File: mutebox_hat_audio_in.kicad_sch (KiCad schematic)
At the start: 23 parts, among them J1 GPIO, U1 CAT24C256, U2 74LVC157, U3 PCM1862DBT

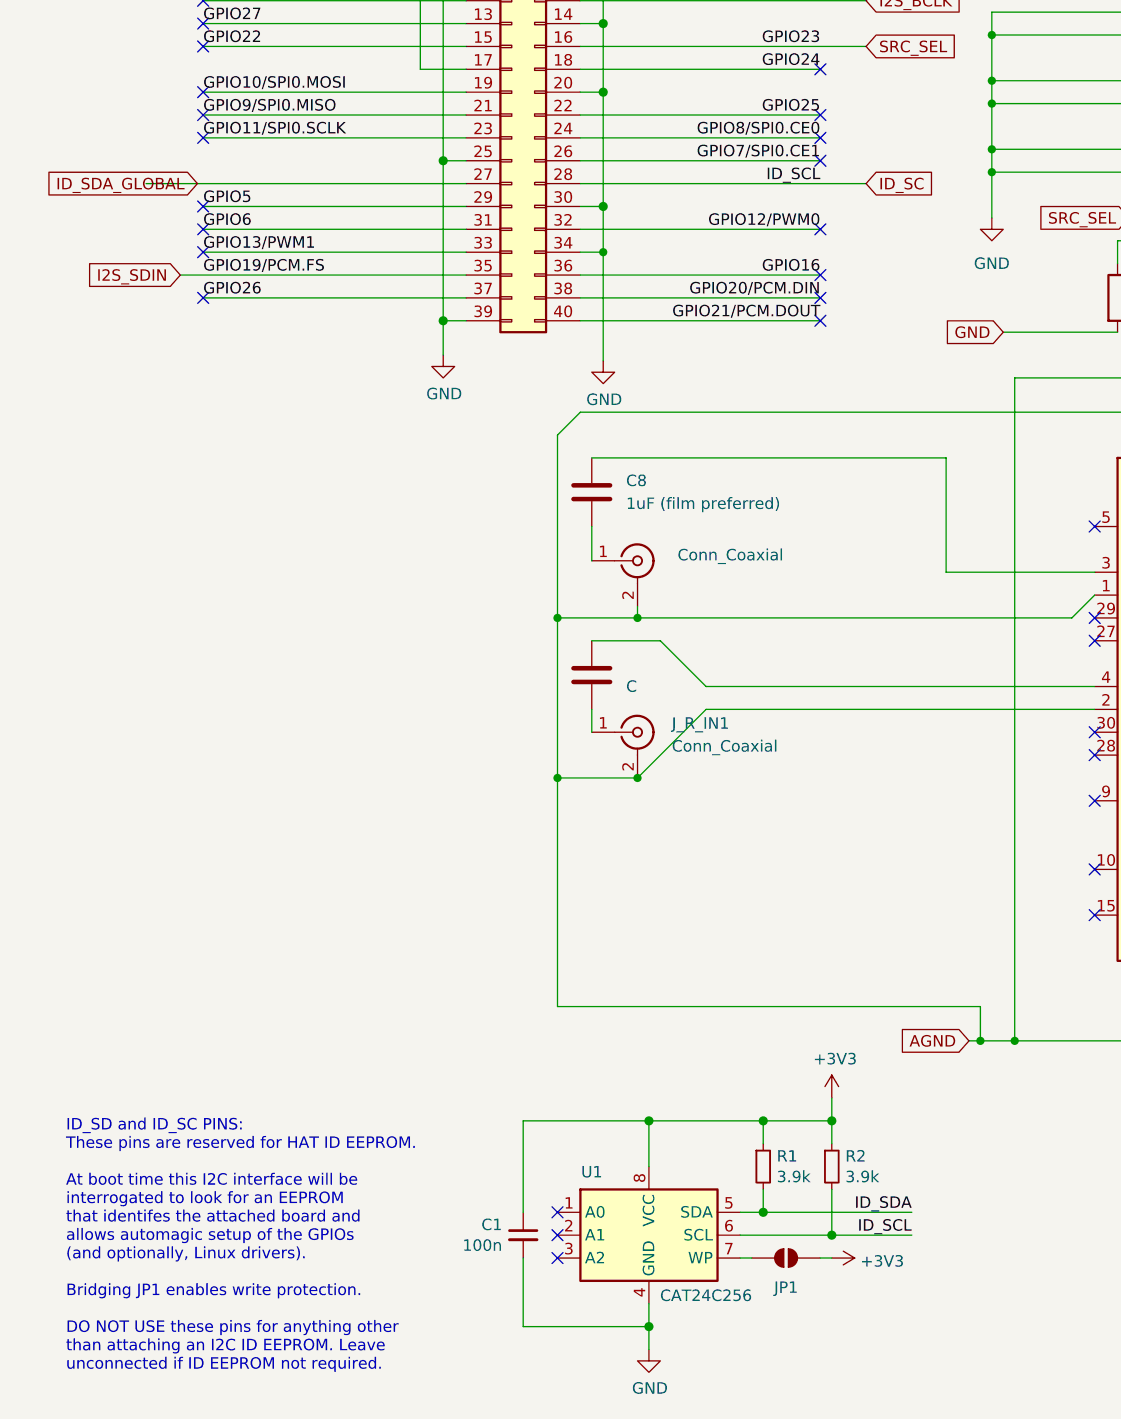
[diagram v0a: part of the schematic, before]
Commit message: Added footprint assignments
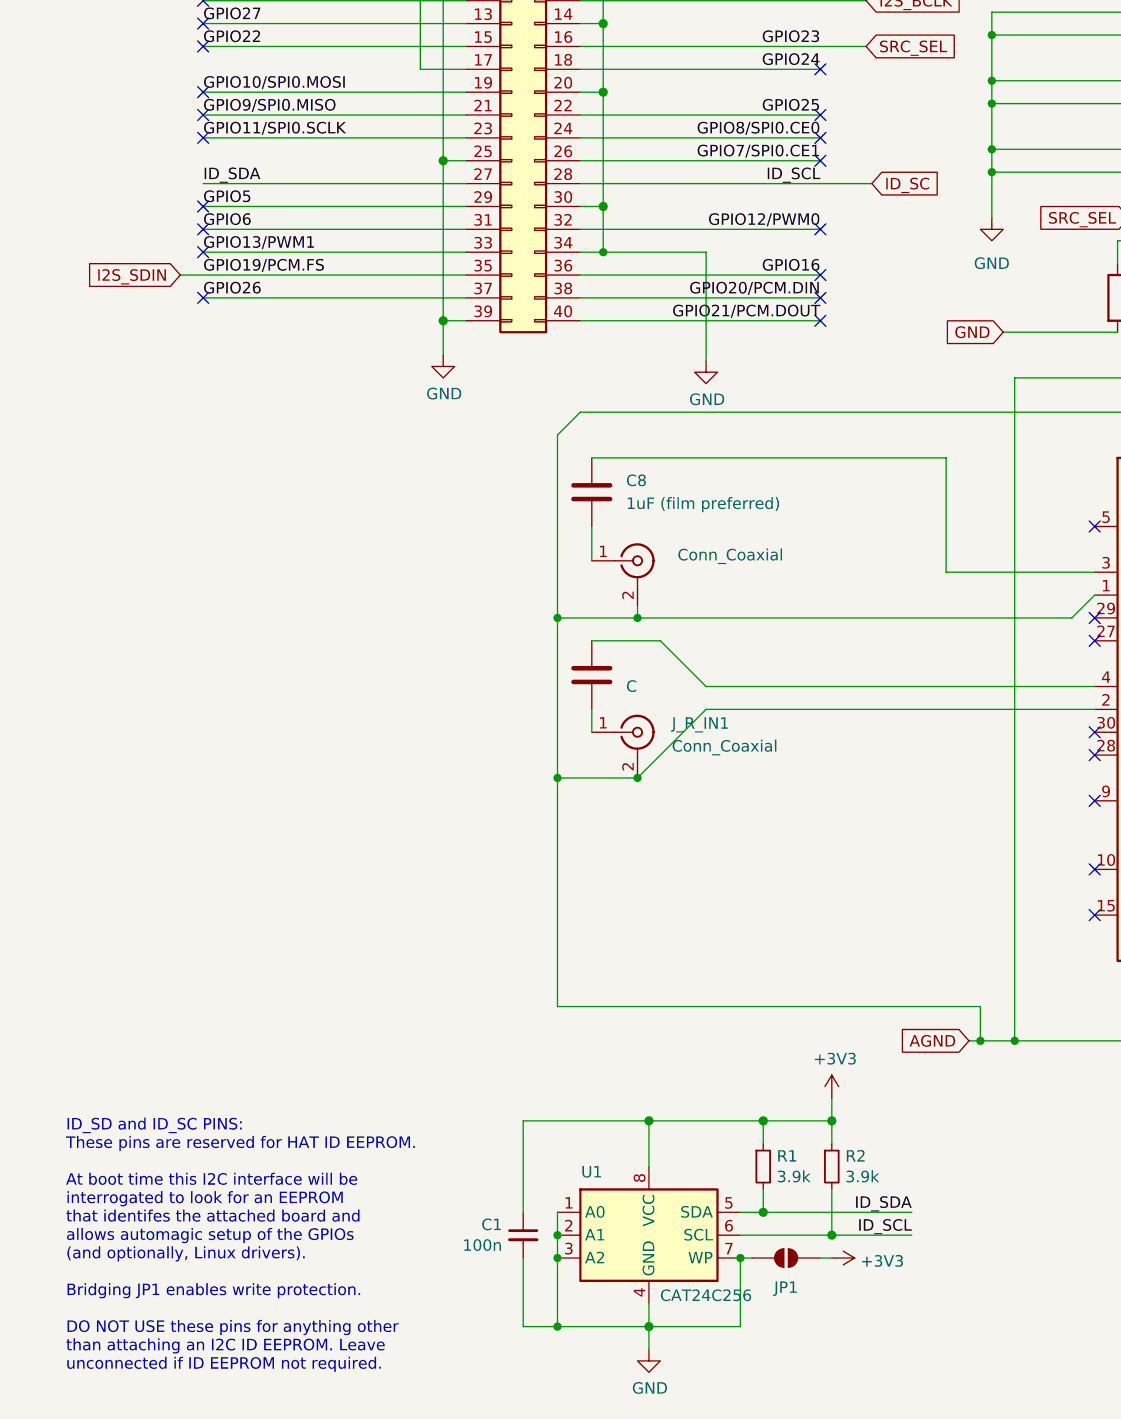
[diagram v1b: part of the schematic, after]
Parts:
- C1, C10, C12, C3, C8, C9, R1, R10, R2, R3, R4, R5, R6, R8, R9: footprint (none) -> Resistor_SMD:R_0805_2012Metric_Pad1.20x1.40mm_HandSolder
- FB1: footprint (none) -> Inductor_SMD:L_0805_2012Metric_Pad1.05x1.20mm_HandSolder
- U1: footprint (none) -> Package_SO:SOIC-8_3.9x4.9mm_P1.27mm
- U2: footprint (none) -> Package_TO_SOT_SMD:SOT-23-5
- U3: footprint Package_SO:TSSOP-30_4.4x7.8mm_P0.5mm -> Package_SO:TSSOP-32_6.1x11mm_P0.65mm
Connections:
- net ID_SDA_GLOBAL is gone; now on net ID_SDA: J1.27 (Pin_27)
- net GND: now also JP1.1 (A), U1.1 (A0), U1.2 (A1), U1.3 (A2), U1.7 (WP)
- no-connect marks 39 -> 36
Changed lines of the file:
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@@
 	)
 	(junction
+		(at 71.12 180.34)
+		(diameter 0)
+		(color 0 0 0 0)
+	)
+	(junction
 		(at 119.38 44.45)
 		(diameter 0)
@@
 	)
 	(junction
+		(at 71.12 187.96)
+		(diameter 0)
+		(color 0 0 0 0)
+	)
+	(junction
+		(at 71.12 177.8)
+		(diameter 0)
+		(color 0 0 0 0)
+	)
+	(junction
 		(at 76.2 63.5)
 		(diameter 1.016)
@@
 	)
 	(junction
+		(at 91.44 180.34)
+		(diameter 0)
+		(color 0 0 0 0)
+	)
+	(junction
 		(at 76.2 33.02)
 		(diameter 0)
@@
 	)
 	(no_connect
-		(at 71.12 175.26)
-	)
-	(no_connect
-		(at 71.12 177.8)
-	)
-	(no_connect
-		(at 71.12 180.34)
-	)
-	(no_connect
 		(at 100.33 53.34)
 	)
@@
 	(wire
 		(pts
-			(xy 25.4 60.96) (xy 60.96 60.96)
-		)
-		(stroke
-			(width 0)
-			(type default)
-		)
-	)
-	(wire
-		(pts
 			(xy 179.07 72.39) (xy 179.07 26.67)
 		)
@@
 	(wire
 		(pts
-			(xy 76.2 68.58) (xy 76.2 80.645)
+			(xy 87.63 68.58) (xy 87.63 80.645)
 		)
 		(stroke
@@
 	(wire
 		(pts
+			(xy 31.75 60.96) (xy 60.96 60.96)
+		)
+		(stroke
+			(width 0)
+			(type default)
+		)
+	)
+	(wire
+		(pts
 			(xy 162.56 34.29) (xy 168.91 34.29)
 		)
@@
 	(wire
 		(pts
+			(xy 71.12 175.26) (xy 71.12 177.8)
+		)
+		(stroke
+			(width 0)
+			(type default)
+		)
+	)
+	(wire
+		(pts
 			(xy 81.28 165.1) (xy 81.28 170.18)
 		)
@@
 	(wire
 		(pts
+			(xy 73.66 60.96) (xy 106.045 60.96)
+		)
+		(stroke
+			(width 0)
+			(type default)
+		)
+	)
+	(wire
+		(pts
 			(xy 193.04 128.27) (xy 193.04 142.24)
 		)
@@
 	(wire
 		(pts
-			(xy 29.21 71.12) (xy 60.96 71.12)
+			(xy 173.99 81.915) (xy 173.99 82.55)
 		)
 		(stroke
 			(width 0)
-			(type solid)
+			(type default)
 		)
 	)
 	(wire
 		(pts
-			(xy 173.99 81.915) (xy 173.99 82.55)
+			(xy 71.12 187.96) (xy 81.28 187.96)
 		)
 		(stroke
 			(width 0)
-			(type default)
+			(type solid)
 		)
 	)
@@
 	(wire
 		(pts
+			(xy 87.63 68.58) (xy 76.2 68.58)
+		)
+		(stroke
+			(width 0)
+			(type default)
+		)
+	)
+	(wire
+		(pts
 			(xy 184.15 128.27) (xy 193.04 128.27)
 		)
@@
 	(wire
 		(pts
+			(xy 71.12 180.34) (xy 71.12 187.96)
+		)
+		(stroke
+			(width 0)
+			(type default)
+		)
+	)
+	(wire
+		(pts
 			(xy 120.65 77.47) (xy 133.35 77.47)
 		)
@@
 	(wire
 		(pts
+			(xy 29.21 71.12) (xy 60.96 71.12)
+		)
+		(stroke
+			(width 0)
+			(type default)
+		)
+	)
+	(wire
+		(pts
 			(xy 67.31 165.1) (xy 67.31 175.26)
 		)
@@
 	(wire
 		(pts
-			(xy 67.31 187.96) (xy 81.28 187.96)
+			(xy 67.31 187.96) (xy 71.12 187.96)
 		)
 		(stroke
@@
 	(wire
 		(pts
+			(xy 91.44 180.34) (xy 91.44 187.96)
+		)
+		(stroke
+			(width 0)
+			(type solid)
+		)
+	)
+	(wire
+		(pts
 			(xy 81.28 185.42) (xy 81.28 187.96)
 		)
@@
 	(wire
 		(pts
+			(xy 71.12 177.8) (xy 71.12 180.34)
+		)
+		(stroke
+			(width 0)
+			(type default)
+		)
+	)
+	(wire
+		(pts
 			(xy 182.88 26.67) (xy 179.07 26.67)
 		)
@@
 	(wire
 		(pts
+			(xy 81.28 187.96) (xy 91.44 187.96)
+		)
+		(stroke
+			(width 0)
+			(type solid)
+		)
+	)
+	(wire
+		(pts
 			(xy 119.38 59.69) (xy 119.38 64.77)
 		)
@@
 	(wire
 		(pts
-			(xy 73.66 60.96) (xy 105.41 60.96)
-		)
-		(stroke
-			(width 0)
-			(type solid)
-		)
-	)
-	(wire
-		(pts
 			(xy 165.1 121.92) (xy 168.91 121.92)
 		)
@@
 		)
 	)
+	(label "ID_SDA"
+		(at 31.75 60.96 0)
+		(effects
+			(font
+				(size 1.27 1.27)
+			)
+			(justify left bottom)
+		)
+	)
 	(label "GPIO4{slash}GPCLK0"
 		(at 31.75 35.56 0)
@@
 		)
 	)
-	(global_label "ID_SDA_GLOBAL"
-		(shape input)
-		(at 31.115 60.96 180)
-		(fields_autoplaced yes)
-		(effects
-			(font
-				(size 1.27 1.27)
-			)
-			(justify right)
-		)
-		(property "Intersheetrefs" "${INTERSHEET_REFS}"
-			(at 13.6413 60.96 0)
-			(effects
-				(font
-					(size 1.27 1.27)
-				)
-				(justify right)
-				(hide yes)
-			)
-		)
-	)
 	(global_label "+3V3"
 		(shape input)
@@
 	(global_label "ID_SC"
 		(shape input)
-		(at 105.41 60.96 0)
+		(at 106.045 60.96 0)
 		(fields_autoplaced yes)
 		(effects
@@
 		)
 		(property "Intersheetrefs" "${INTERSHEET_REFS}"
-			(at 113.8122 60.96 0)
+			(at 114.4472 60.96 0)
 			(effects
 				(font
@@
 	(symbol
 		(lib_id "power:GND")
-		(at 76.2 80.645 0)
+		(at 87.63 80.645 0)
 		(unit 1)
 		(exclude_from_sim no)
@@
 		(dnp no)
 		(property "Reference" "#PWR02"
-			(at 76.2 86.995 0)
+			(at 87.63 86.995 0)
 			(effects
 				(font
@@
 		)
 		(property "Value" "GND"
-			(at 76.3143 84.9694 0)
+			(at 87.7443 84.9694 0)
 			(effects
 				(font
@@
 		)
 		(property "Footprint" ""
-			(at 76.2 80.645 0)
+			(at 87.63 80.645 0)
 			(effects
 				(font
@@
 		)
 		(property "Datasheet" ""
-			(at 76.2 80.645 0)
+			(at 87.63 80.645 0)
 			(effects
 				(font
@@
 		)
 		(property "Description" "Power symbol creates a global label with name \"GND\" , ground"
-			(at 76.2 80.645 0)
+			(at 87.63 80.645 0)
 			(effects
 				(font
@@
 			)
 		)
-		(property "Footprint" ""
+		(property "Footprint" "Resistor_SMD:R_0805_2012Metric_Pad1.20x1.40mm_HandSolder"
 			(at 67.31 177.8 0)
 			(effects
@@
 			)
 		)
-		(property "Footprint" ""
+		(property "Footprint" "Resistor_SMD:R_0805_2012Metric_Pad1.20x1.40mm_HandSolder"
 			(at 27.94 34.798 90)
 			(effects
@@
 			)
 		)
-		(property "Footprint" ""
+		(property "Footprint" "Resistor_SMD:R_0805_2012Metric_Pad1.20x1.40mm_HandSolder"
 			(at 75.8952 99.06 0)
 			(effects
@@
 			)
 		)
-		(property "Footprint" ""
+		(property "Footprint" "Resistor_SMD:R_0805_2012Metric_Pad1.20x1.40mm_HandSolder"
 			(at 93.98 170.18 0)
 			(effects
@@
 			)
 		)
-		(property "Footprint" ""
+		(property "Footprint" "Resistor_SMD:R_0805_2012Metric_Pad1.20x1.40mm_HandSolder"
 			(at 101.6 170.18 0)
 			(effects
@@
 			)
 		)
-		(property "Footprint" ""
+		(property "Footprint" "Resistor_SMD:R_0805_2012Metric_Pad1.20x1.40mm_HandSolder"
 			(at 75.8952 119.38 0)
 			(effects
@@
 			)
 		)
-		(property "Footprint" ""
+		(property "Footprint" "Resistor_SMD:R_0805_2012Metric_Pad1.20x1.40mm_HandSolder"
 			(at 180.0352 99.06 0)
 			(effects
@@
 			)
 		)
-		(property "Footprint" ""
+		(property "Footprint" "Package_SO:SOIC-8_3.9x4.9mm_P1.27mm"
 			(at 81.28 177.8 0)
 			(effects
@@
 			)
 		)
-		(property "Footprint" "Package_SO:TSSOP-30_4.4x7.8mm_P0.5mm"
+		(property "Footprint" "Package_SO:TSSOP-32_6.1x11mm_P0.65mm"
 			(at 151.384 151.384 0)
 			(effects
@@
 			)
 		)
-		(property "Footprint" ""
+		(property "Footprint" "Resistor_SMD:R_0805_2012Metric_Pad1.20x1.40mm_HandSolder"
 			(at 169.8752 148.59 0)
 			(effects
@@
 			)
 		)
-		(property "Footprint" ""
+		(property "Footprint" "Inductor_SMD:L_0805_2012Metric_Pad1.05x1.20mm_HandSolder"
 			(at 177.292 76.2 90)
 			(effects
@@
 			)
 		)
-		(property "Footprint" ""
+		(property "Footprint" "Resistor_SMD:R_0805_2012Metric_Pad1.20x1.40mm_HandSolder"
 			(at 195.072 146.05 90)
 			(effects
@@
 			)
 		)
-		(property "Footprint" ""
+		(property "Footprint" "Resistor_SMD:R_0805_2012Metric_Pad1.20x1.40mm_HandSolder"
 			(at 186.182 146.05 90)
 			(effects
@@
 			)
 		)
-		(property "Footprint" ""
+		(property "Footprint" "Resistor_SMD:R_0805_2012Metric_Pad1.20x1.40mm_HandSolder"
 			(at 168.6052 99.06 0)
 			(effects
@@
 			)
 		)
-		(property "Footprint" ""
+		(property "Footprint" "Resistor_SMD:R_0805_2012Metric_Pad1.20x1.40mm_HandSolder"
 			(at 27.94 32.258 90)
 			(effects
@@
 			)
 		)
-		(property "Footprint" ""
+		(property "Footprint" "Package_TO_SOT_SMD:SOT-23-5"
 			(at 149.86 49.53 0)
 			(effects
@@
 			)
 		)
-		(property "Footprint" ""
+		(property "Footprint" "Resistor_SMD:R_0805_2012Metric_Pad1.20x1.40mm_HandSolder"
 			(at 131.572 73.66 90)
 			(effects
@@
 			)
 		)
-		(property "Footprint" ""
+		(property "Footprint" "Resistor_SMD:R_0805_2012Metric_Pad1.20x1.40mm_HandSolder"
 			(at 191.262 146.05 90)
 			(effects
@@
 			)
 		)
-		(property "Footprint" ""
+		(property "Footprint" "Resistor_SMD:R_0805_2012Metric_Pad1.20x1.40mm_HandSolder"
 			(at 179.832 146.05 90)
 			(effects

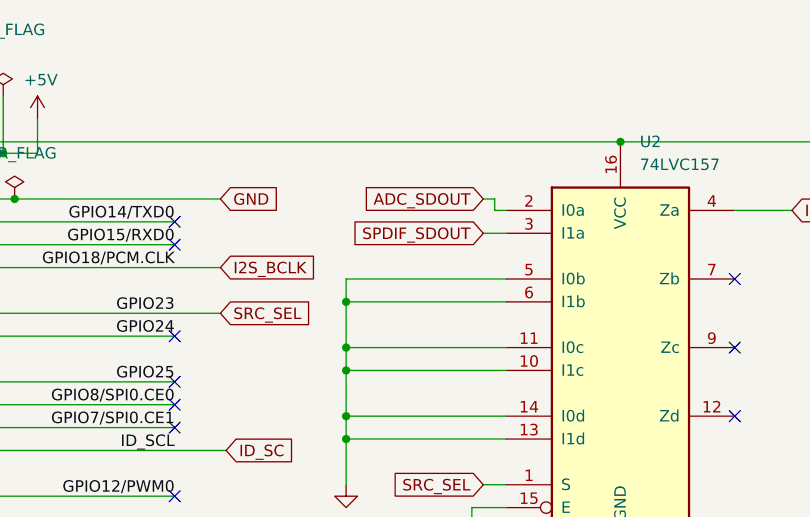
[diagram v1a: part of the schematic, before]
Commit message: switched to DIR9001PW for digital audio input
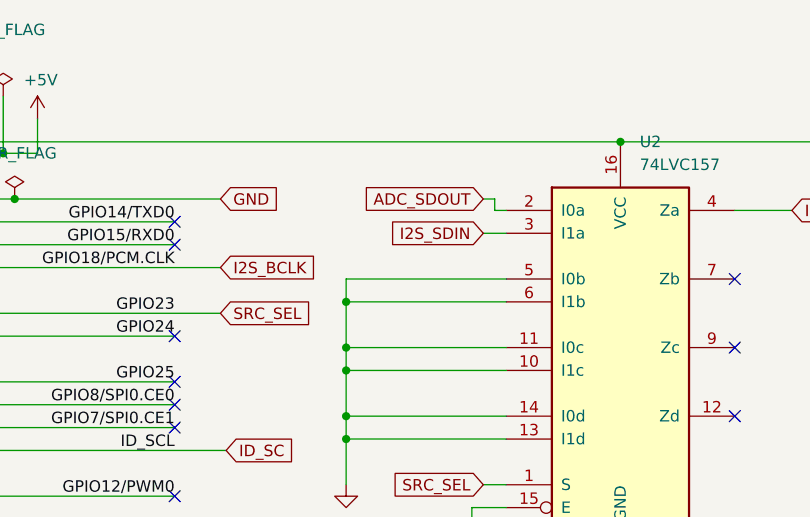
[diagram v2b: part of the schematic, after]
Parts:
- U2: footprint Package_TO_SOT_SMD:SOT-23-5 -> Package_SO:SOIC-16_3.9x9.9mm_P1.27mm
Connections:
- net SPDIF_SDOUT is gone; now on net I2S_SDIN: U2.3 (I1a)
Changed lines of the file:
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@@
 		)
 	)
-	(global_label "SPDIF_SDOUT"
+	(global_label "I2S_SDIN"
 		(shape input)
 		(at 134.62 36.83 180)
@@
 		)
 		(property "Intersheetrefs" "${INTERSHEET_REFS}"
-			(at 150.2189 36.83 0)
-			(effects
-				(font
-					(size 1.27 1.27)
-				)
-				(justify left)
+			(at 123.1335 36.83 0)
+			(effects
+				(font
+					(size 1.27 1.27)
+				)
+				(justify right)
 				(hide yes)
 			)
@@
 			)
 		)
-		(property "Footprint" "Package_TO_SOT_SMD:SOT-23-5"
+		(property "Footprint" "Package_SO:SOIC-16_3.9x9.9mm_P1.27mm"
 			(at 149.86 49.53 0)
 			(effects

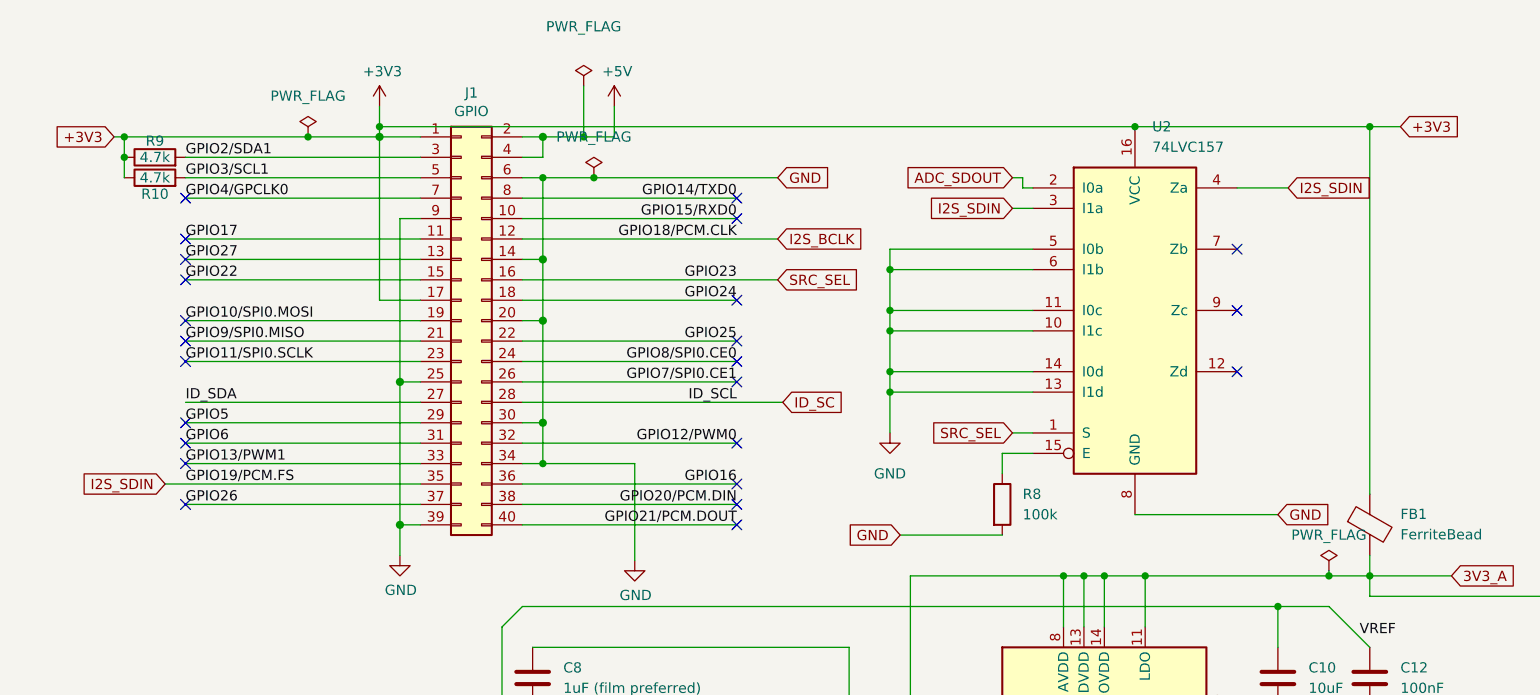
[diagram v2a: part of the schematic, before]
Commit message: Fixed some errors, like power connections
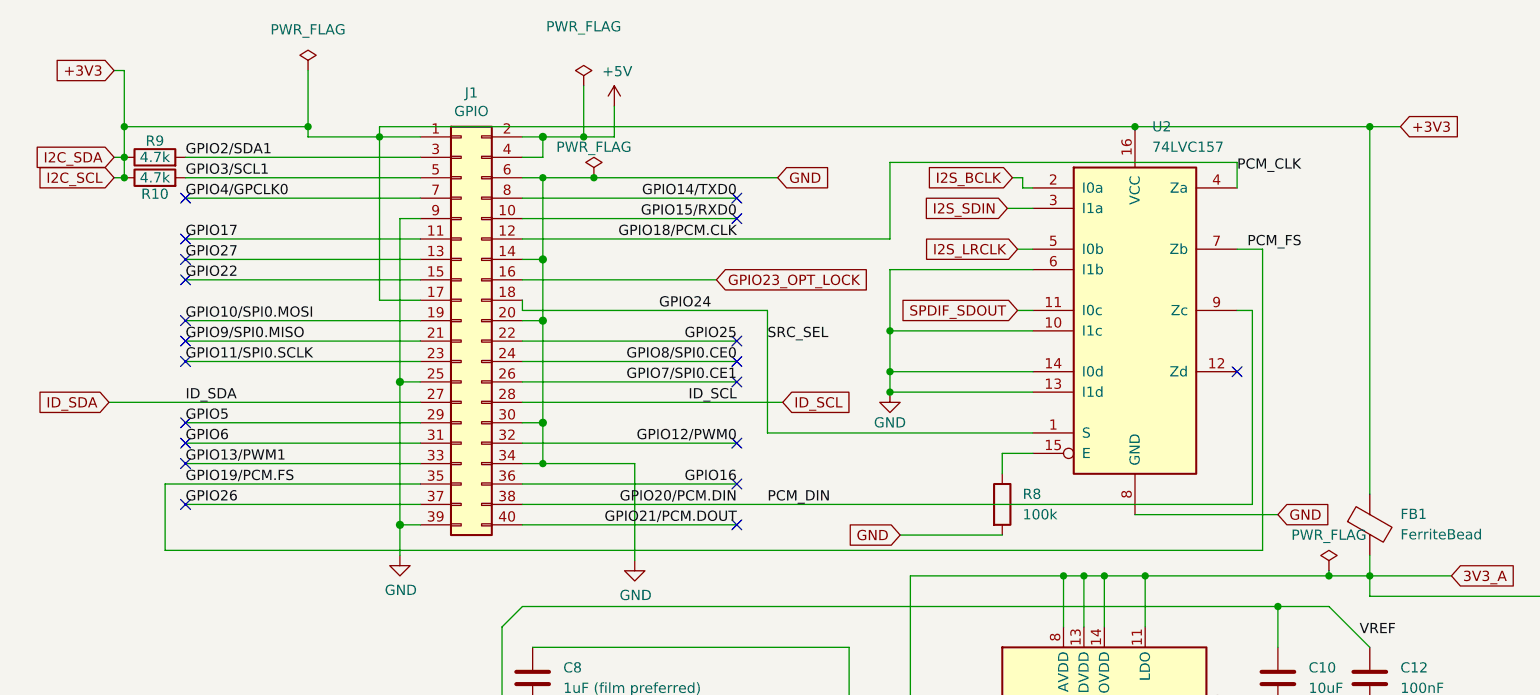
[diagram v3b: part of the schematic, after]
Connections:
- net ADC_SDOUT: no longer U2.2 (I0a)
- net GND: no longer U2.11 (I0c), U2.5 (I0b)
- net GPIO20/PCM.DIN: now also U2.9 (Zc)
- net GPIO24: now also U2.1 (S)
- net I2S_BCLK: now also U2.2 (I0a); no longer J1.12 (Pin_12)
- net I2S_LRCLK: now also U2.5 (I0b)
- net I2S_SDIN: no longer J1.35 (Pin_35), U2.4 (Za)
- net GPIO19/PCM.FS: now reaches U2.7 (Zb)
- net GPIO19/PCM.FS: now also J1.35 (Pin_35)
- net ID_SC renamed ID_SCL
- net SRC_SEL renamed GPIO23_OPT_LOCK
- net GPIO23_OPT_LOCK: no longer U2.1 (S)
- new net GPIO18/PCM.CLK: J1.12 (Pin_12), U2.4 (Za)
- new net SPDIF_SDOUT: U2.11 (I0c)
- no-connect marks 36 -> 32
